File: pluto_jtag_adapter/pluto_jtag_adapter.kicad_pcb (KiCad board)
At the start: 2 copper layers, 50 parts, among them J1 JTAG_UART_PLUTO, J2 Conn_01x08, J3 Conn_01x04, J4 USB_B_Micro, U1 FT2232HL, U2 AP2112K-3.3, U3 AP2112K-1.8, U4 93LC46B, U5 TXB0102DCT, U6 TXB0104D, Y1 7M-12.000MAAJ-T

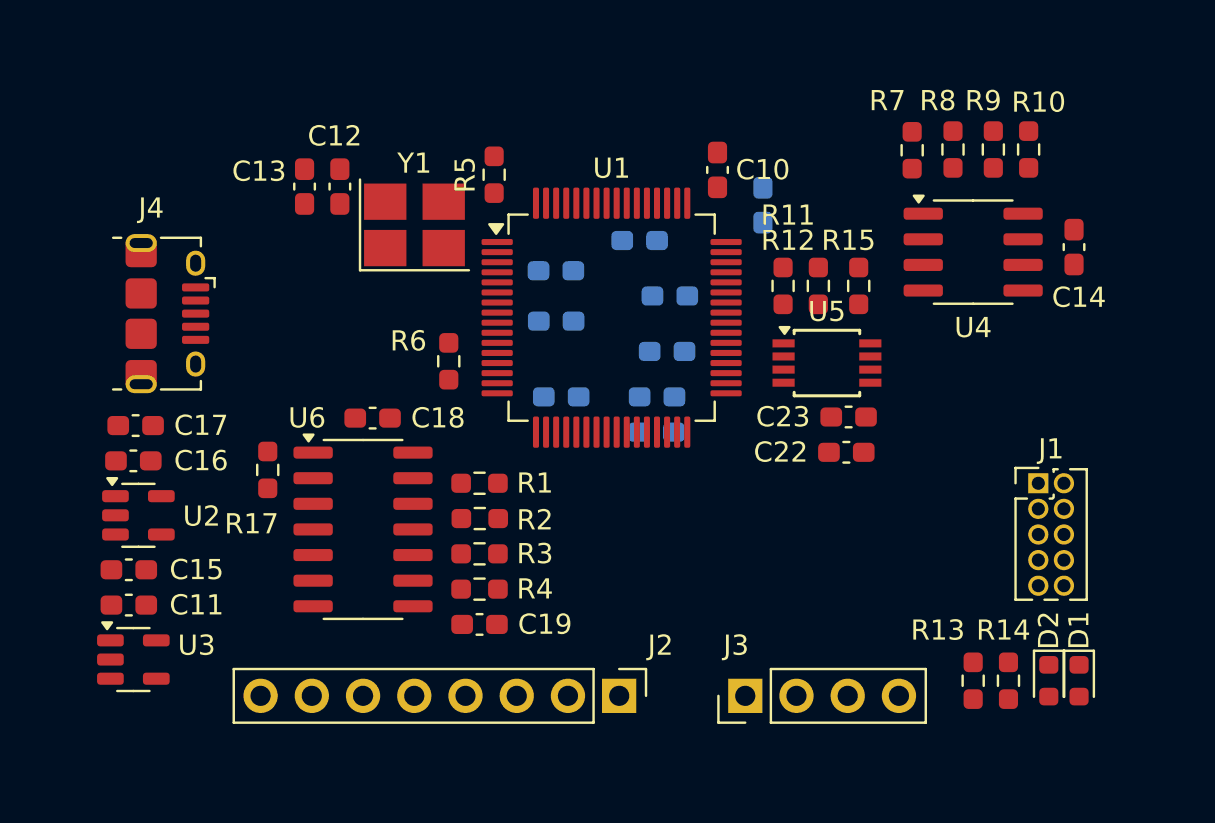
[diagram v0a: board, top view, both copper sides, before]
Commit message: Clean up PCB layout, add mounting holes and header pin names
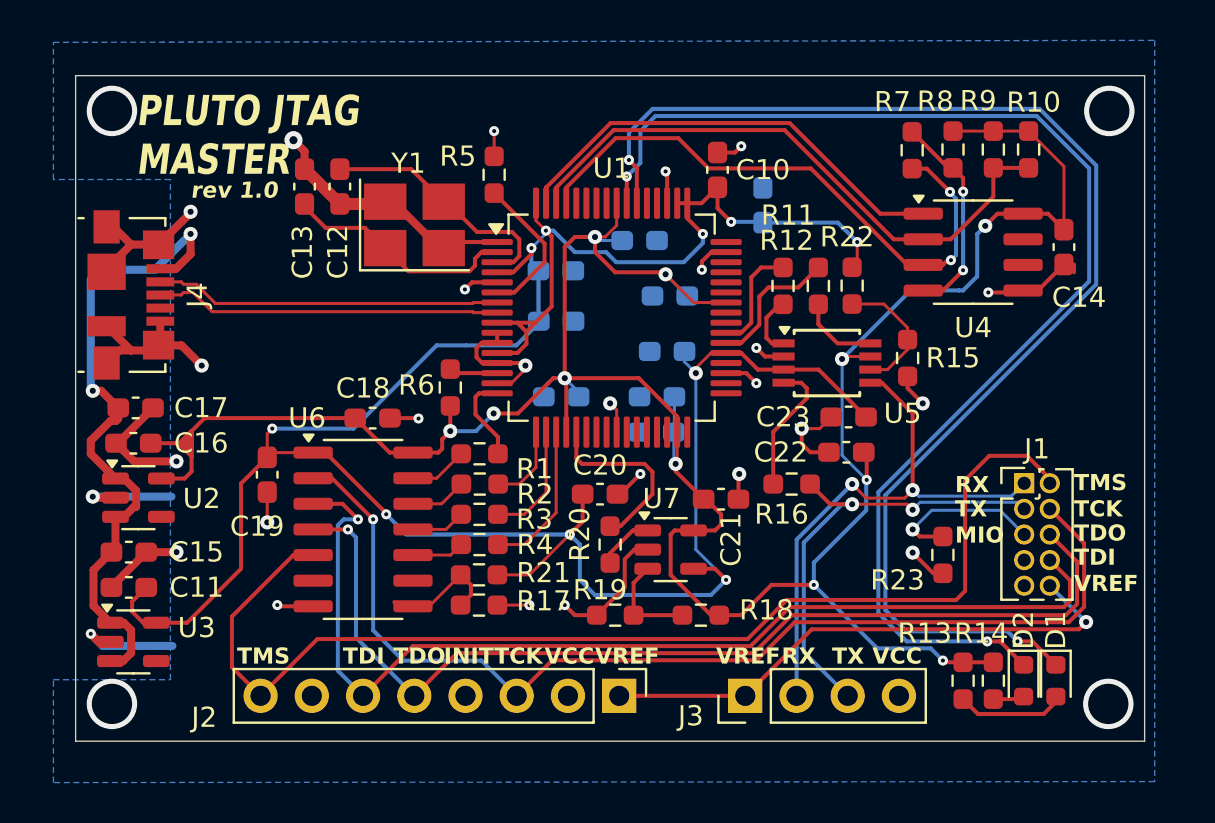
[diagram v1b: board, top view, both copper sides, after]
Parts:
- added C20: 100n, Capacitor_SMD:C_0603_1608Metric_Pad1.08x0.95mm_HandSolder, F.Cu at (120.0, 100.0)
- added C21: 100n, Capacitor_SMD:C_0603_1608Metric_Pad1.08x0.95mm_HandSolder, F.Cu at (126.0, 100.2)
- added R16: 33, Resistor_SMD:R_0603_1608Metric_Pad0.98x0.95mm_HandSolder, F.Cu at (129.5, 99.5)
- added R18: 2K, Resistor_SMD:R_0603_1608Metric_Pad0.98x0.95mm_HandSolder, F.Cu at (125.0, 106.0)
- added R19: 1K, Resistor_SMD:R_0603_1608Metric_Pad0.98x0.95mm_HandSolder, F.Cu at (120.8, 106.0)
- added R20: 0, Resistor_SMD:R_0603_1608Metric_Pad0.98x0.95mm_HandSolder, F.Cu at (120.5, 102.5)
- added R21: 0, Resistor_SMD:R_0603_1608Metric_Pad0.98x0.95mm_HandSolder, F.Cu at (114.0, 104.0)
- added R22: 0, Resistor_SMD:R_0603_1608Metric_Pad0.98x0.95mm_HandSolder, F.Cu at (132.5, 89.7)
- added R23: 0, Resistor_SMD:R_0603_1608Metric_Pad0.98x0.95mm_HandSolder, F.Cu at (137.0, 103.0)
- added U7: TLV7031DBV, Package_TO_SOT_SMD:SOT-23-5, F.Cu at (123.5, 102.8)
- J4: footprint Connector_USB:USB_Micro-B_Amphenol_10118194_Horizontal -> Connector_USB:USB_Micro-B_Molex_47346-0001
- moved C19 12.9 mm to (103.5, 99.0), turned to -90 degrees
- moved R17 12.4 mm to (114.0, 105.5), turned to 0 degrees
- moved R15 4.32 mm to (135.2, 93.2)
- moved R4 2.21 mm to (114.0, 102.5)
- moved J4 2.03 mm to (96.7, 90.1)
- moved R3 1.96 mm to (114.0, 101.0)
- moved R2 1.71 mm to (114.0, 99.5)
- moved R1 1.46 mm to (114.0, 98.0)
- moved R6 1.30 mm to (112.6, 94.7)
- moved D2 1.25 mm to (141.0, 109.2)
- moved D1 1.15 mm to (142.6, 109.2)
- moved C11 0.88 mm to (96.6, 104.6)
- moved C15 0.88 mm to (96.6, 102.9)
- moved C16 0.88 mm to (96.9, 97.5)
- moved C17 0.88 mm to (97.0, 95.7)
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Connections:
- net Net-(J4-D+) renamed /D+
- net Net-(J4-D-) renamed /D-
- R15 pad 1: +1V8 -> Net-(U5-OE)
- R17 pad 1: +1V8 -> Net-(U6-OE)
- U1 pad 21: unconnected-(U1-ADBUS4-Pad21) -> Net-(U1-ADBUS4)
- U5 pad 4: UART_TX -> Net-(U5-A2)
- U5 pad 6: +1V8 -> Net-(U5-OE)
- U6 pad 8: +1V8 -> Net-(U6-OE)
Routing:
- net +3.3V: track 0.00 -> 136.4 mm, vias 0 -> 11
- net +1V8: track 0.00 -> 132.3 mm, vias 0 -> 10
- net GND: track 0.00 -> 95.9 mm, vias 0 -> 31
- net RXLED: track 0.00 -> 64.4 mm, vias 0 -> 2
- net TXLED: track 0.00 -> 62.1 mm, vias 0 -> 2
- net JTAG_TMS: track 0.00 -> 57.9 mm
- net JTAG_TCK: track 0.00 -> 53.3 mm, vias 0 -> 1
- net JTAG_TDI: track 0.00 -> 52.1 mm, vias 0 -> 1
- net JTAG_TDO: track 0.00 -> 50.1 mm, vias 0 -> 1
- net Net-(J4-VBUS): track 0.00 -> 33.4 mm, vias 0 -> 2
- net Net-(U1-EECLK): track 0.00 -> 29.9 mm
- net Net-(U1-EEDATA): track 0.00 -> 29.5 mm, vias 0 -> 2
- net UART_RX: track 0.00 -> 27.5 mm, vias 0 -> 2
- net VREF: track 0.00 -> 27.2 mm, vias 0 -> 1
- net UART_TX: track 0.00 -> 23.1 mm, vias 0 -> 2
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- added copper zone on B.Cu, net GND
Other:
- board outline added: 53 x 33 mm
- board text added: "INIT"
- board text added: "MIO"
- board text added: "PLUTO JTAG MASTER"
- board text added: "RX"
- board text added: "TCK"
- board text added: "TDI"
- board text added: "TDO"
- board text added: "TMS"
- board text added: "TX"
- board text added: "VCC"
- board text added: "VREF"
- board text added: "rev 1.0"

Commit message: Clean up layout based on first round of design feedback
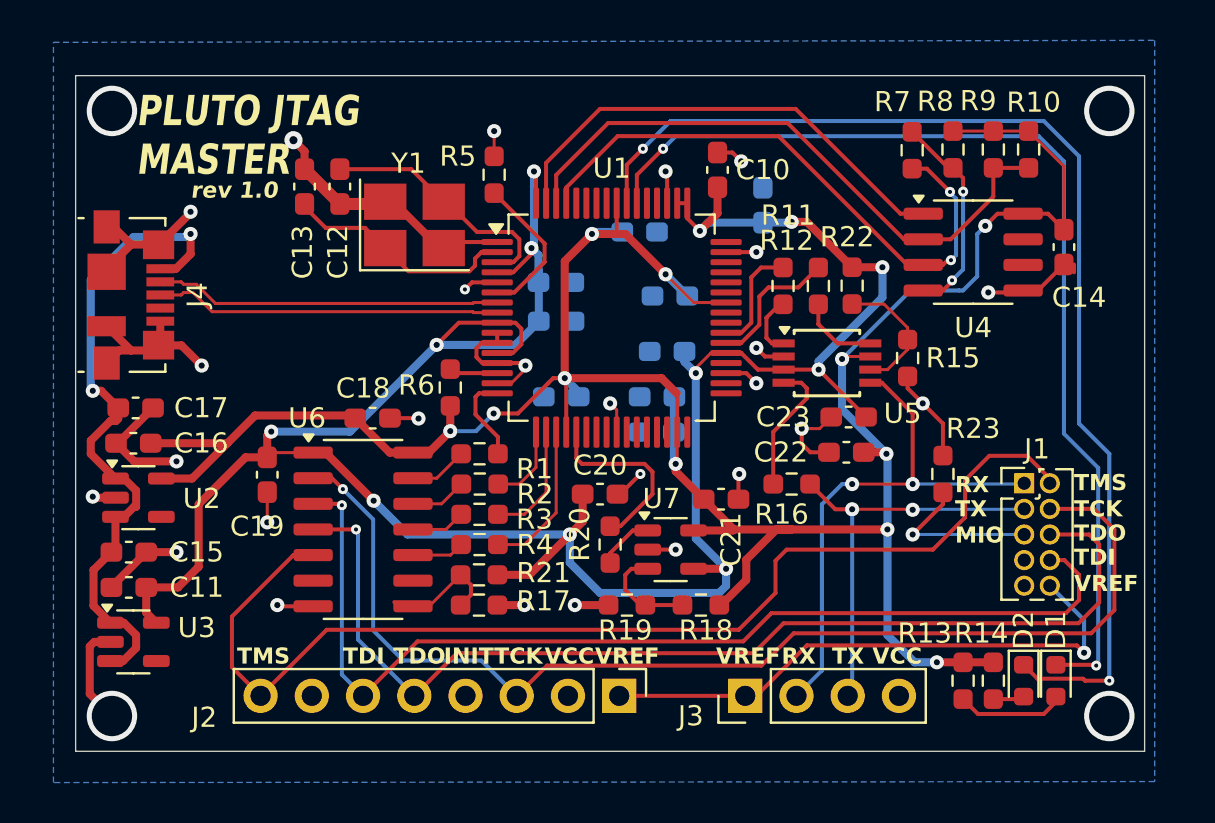
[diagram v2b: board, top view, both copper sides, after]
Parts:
- moved R23 4.01 mm to (137.0, 99.0), turned to -90 degrees
- moved R19 0.77 mm to (121.3, 105.5)
- moved C1 0.58 mm to (117.8, 89.5)
- moved R18 0.50 mm to (125.0, 105.5)
- moved C4 0.42 mm to (122.0, 87.0)
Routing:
- net RXLED: track 64.4 -> 51.7 mm
- net GND: track 95.9 -> 88.7 mm, vias 31 -> 30
- net TXLED: track 62.1 -> 57.1 mm
- net +1V8: track 132.3 -> 128.1 mm, vias 10 -> 12
- net JTAG_TCK: track 53.3 -> 56.8 mm
- net JTAG_TDO: track 50.1 -> 53.0 mm
- net UART_TX: track 23.1 -> 20.5 mm
- net +3.3V: track 136.4 -> 133.9 mm
- net Net-(U1-EECS): track 22.7 -> 24.0 mm
- net JTAG_TMS: track 57.9 -> 56.7 mm
- net VREF: track 27.2 -> 28.3 mm
- net UART_RX: track 27.5 -> 26.7 mm
- net Net-(U1-EECLK): track 29.9 -> 30.6 mm
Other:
- board size 53 x 33 mm -> 53 x 33.5 mm

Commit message: Add ground fill on top layer. Improve ground fill around signals
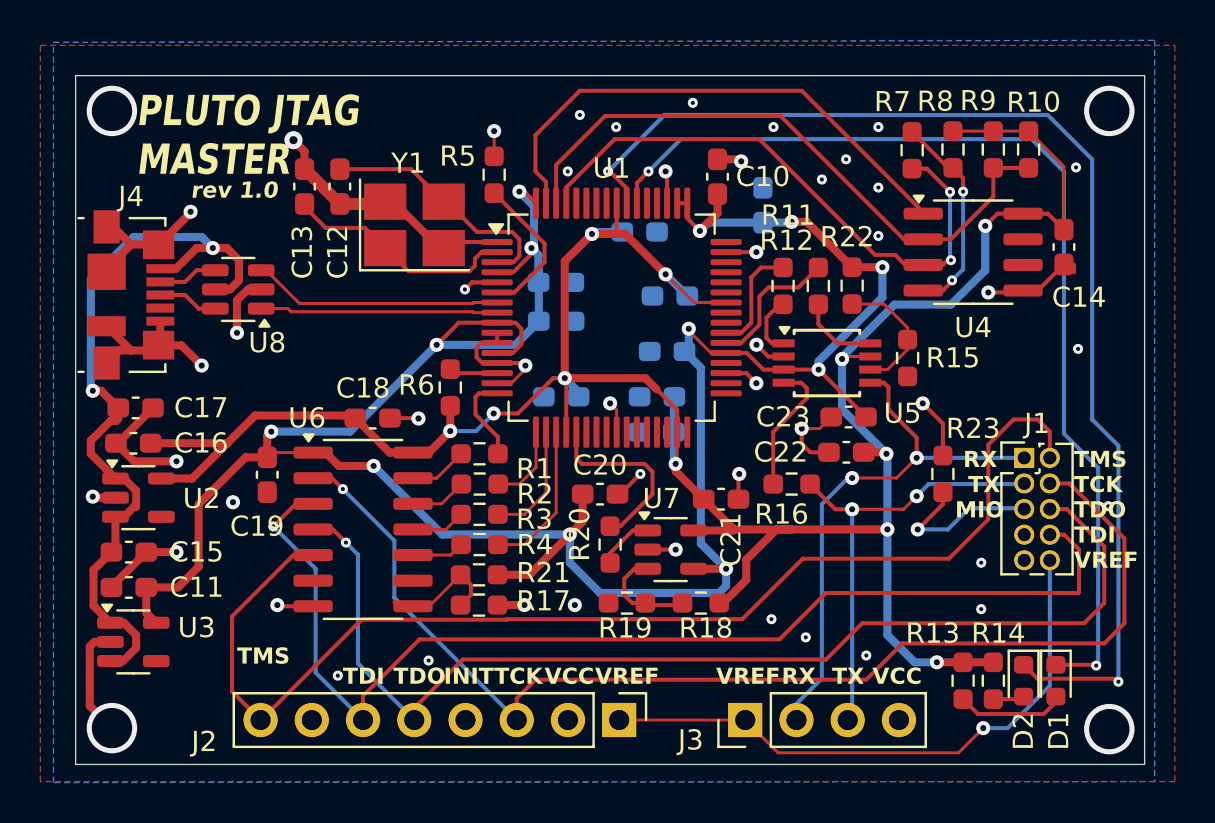
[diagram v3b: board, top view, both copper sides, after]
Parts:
- added U8: WE-TVS-82400102, Package_TO_SOT_SMD:SOT-23-6, F.Cu at (102.1, 89.8)
- moved J1 1.26 mm to (141.0, 98.2)
- moved J2 1.20 mm to (121.0, 111.2)
- moved J3 1.20 mm to (127.2, 111.2)
- moved C10 0.34 mm to (125.8, 84.3)
- moved R18 0.10 mm to (125.0, 105.4)
- moved R19 0.10 mm to (121.3, 105.4)
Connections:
- net Net-(J4-VBUS) renamed /USB_VBUS
- J4 pad 2: /D- -> /USB_TVS_N
- J4 pad 3: /D+ -> /USB_TVS_P
- U1 pad 7: /D- -> /USB_N
- U1 pad 8: /D+ -> /USB_P
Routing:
- net /D+: track 17.8 -> 0.00 mm
- net /D-: track 17.4 -> 0.00 mm
- net /USB_P: track 0.00 -> 12.4 mm
- net /USB_N: track 0.00 -> 12.4 mm
- net /USB_VBUS: track 33.6 -> 39.0 mm
- net JTAG_TDI: track 51.8 -> 56.6 mm
- net JTAG_TMS: track 56.7 -> 60.0 mm
- net /USB_TVS_N: track 0.00 -> 3.18 mm
- net /USB_TVS_P: track 0.00 -> 3.01 mm
- net TXLED: track 57.1 -> 59.6 mm
- net JTAG_TDO: track 53.0 -> 55.3 mm
- net Net-(U1-EECS): track 24.0 -> 26.3 mm
- net UART_TX: track 20.5 -> 22.2 mm
- net JTAG_TCK: track 56.8 -> 58.5 mm
- net VREF: track 28.3 -> 29.6 mm
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- added copper zone on F.Cu, net GND
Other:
- board size 53 x 33.5 mm -> 53 x 34.2 mm

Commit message: Move oscillator caps closer to oscillator
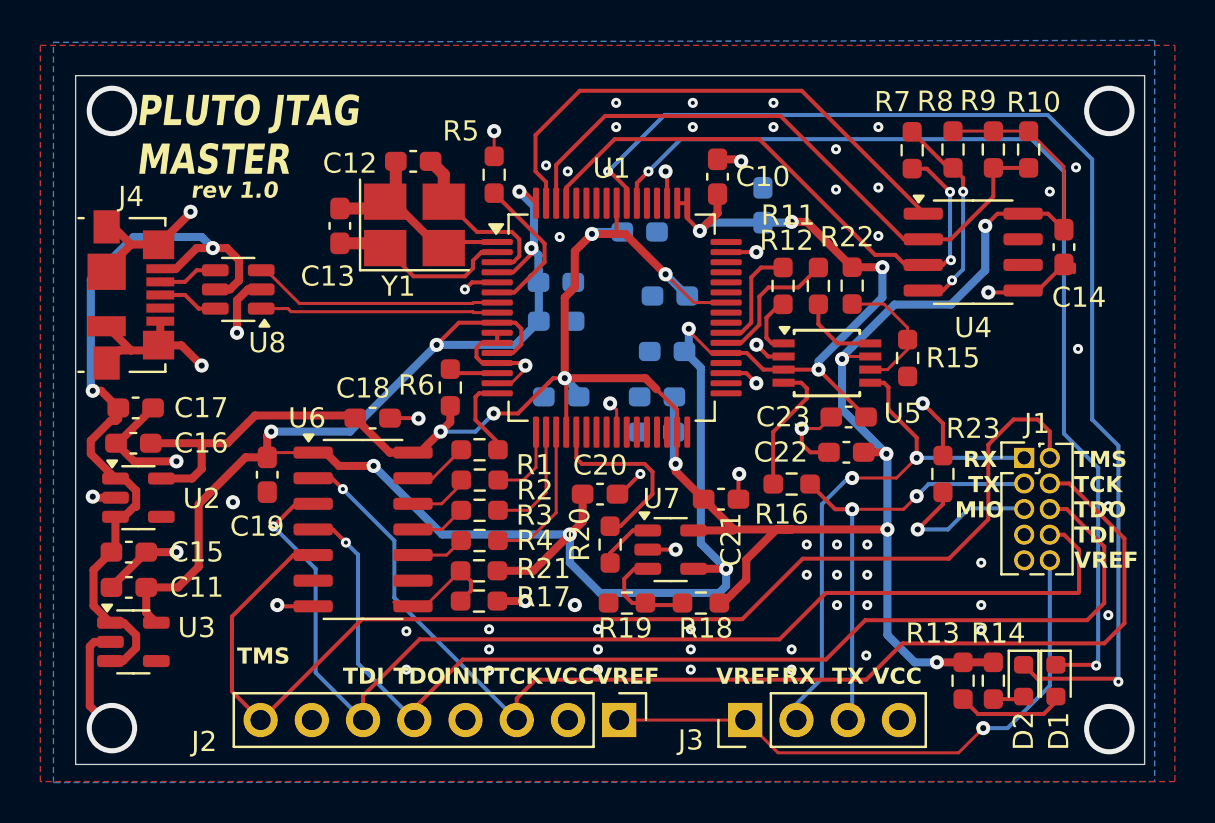
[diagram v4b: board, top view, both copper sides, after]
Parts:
- moved C12 3.85 mm to (110.7, 83.5), turned to 0 degrees
- moved C13 2.62 mm to (107.1, 86.7)
- moved R1 0.20 mm to (114.0, 97.8)
- moved R17 0.20 mm to (114.0, 105.3)
- moved R2 0.20 mm to (114.0, 99.3)
- moved R21 0.20 mm to (114.0, 103.8)
- moved R3 0.20 mm to (114.0, 100.8)
- moved R4 0.20 mm to (114.0, 102.3)
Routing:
- net Net-(U1-OSCO): track 12.4 -> 8.85 mm
- net Net-(U1-OSCI): track 11.6 -> 9.20 mm
- net GND: track 87.9 -> 86.1 mm, vias 51 -> 74

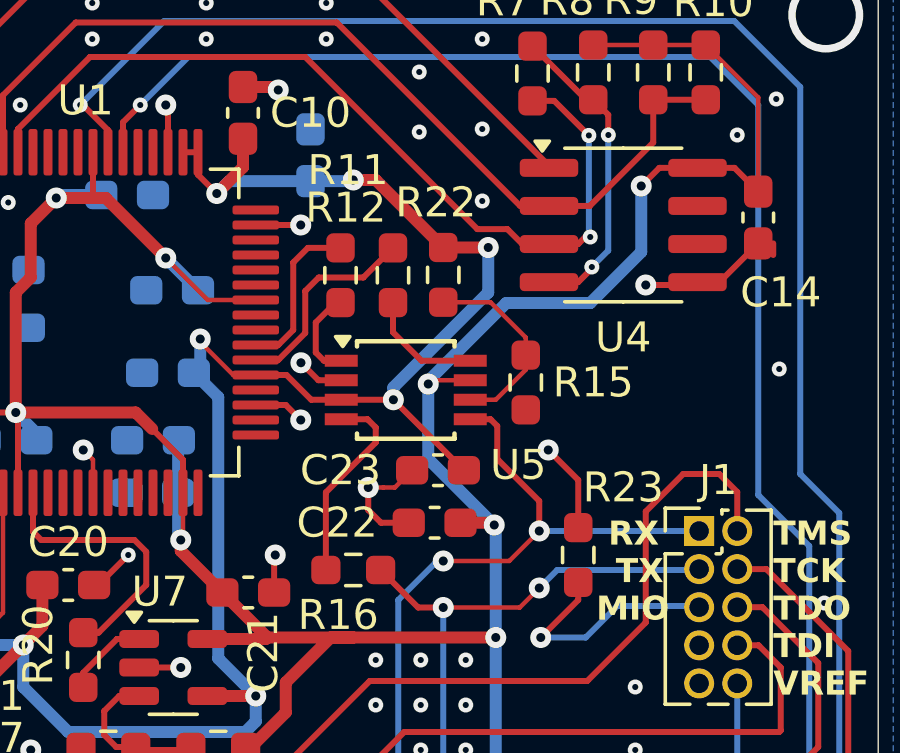
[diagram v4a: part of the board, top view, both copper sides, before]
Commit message: Replace obsolete component TXB0102DCT with TXB0102DCU
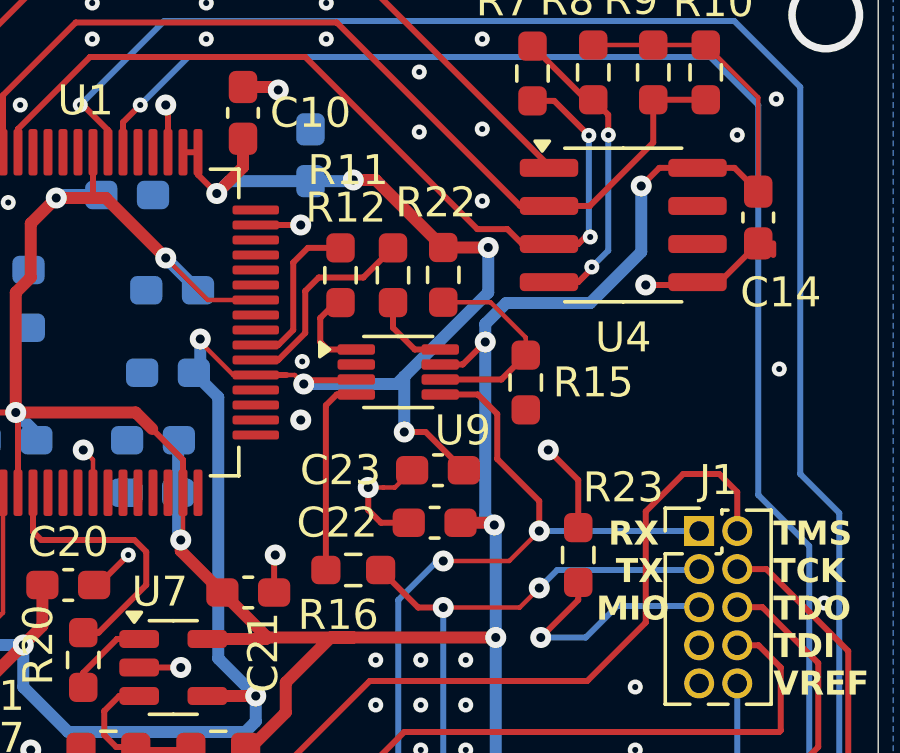
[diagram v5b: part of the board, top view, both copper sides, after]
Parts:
- removed U5: TXB0102DCT, Package_SO:TSSOP-8_3x3mm_P0.65mm
- added U9: TXB0102DCU, Package_SO:VSSOP-8_2.3x2mm_P0.5mm, F.Cu at (131.0, 92.9)
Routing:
- net GND: track 86.1 -> 82.8 mm
- net +1V8: track 128.0 -> 129.6 mm, vias 12 -> 13
- net UART_RX: track 26.5 -> 28.1 mm
- net Net-(U9-B1): track 3.96 -> 2.71 mm
- net +3.3V: track 133.2 -> 132.0 mm
